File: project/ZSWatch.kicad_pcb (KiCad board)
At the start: 4 copper layers, 41 x 38 mm, 92 parts, among them IC101 nPM1300-QEXX, IC201 APDS-9306-065, IC202 BMI270, IC203 BMP581, IC204 LIS2MDLTR, IC205 BME688, IC301 ESDALC6V1W5, IC302 FAN5622SX, IC303 MX25U51245GZ4I00, IC304 TS3USB221A, IC305 NTS0104GU12, IC306 DRV2603RUNT, IC307 RV-8263-C8, M301 NORA-B106, Q201 DMG1013UW-7, Q301 BC817W, Q302 PMZ550UNEYL, Q303 PMZ550UNEYL, X101 BATTERY, X301 DOCK, X302 GC9A01A_CST816S, X303 M+, X304 M-

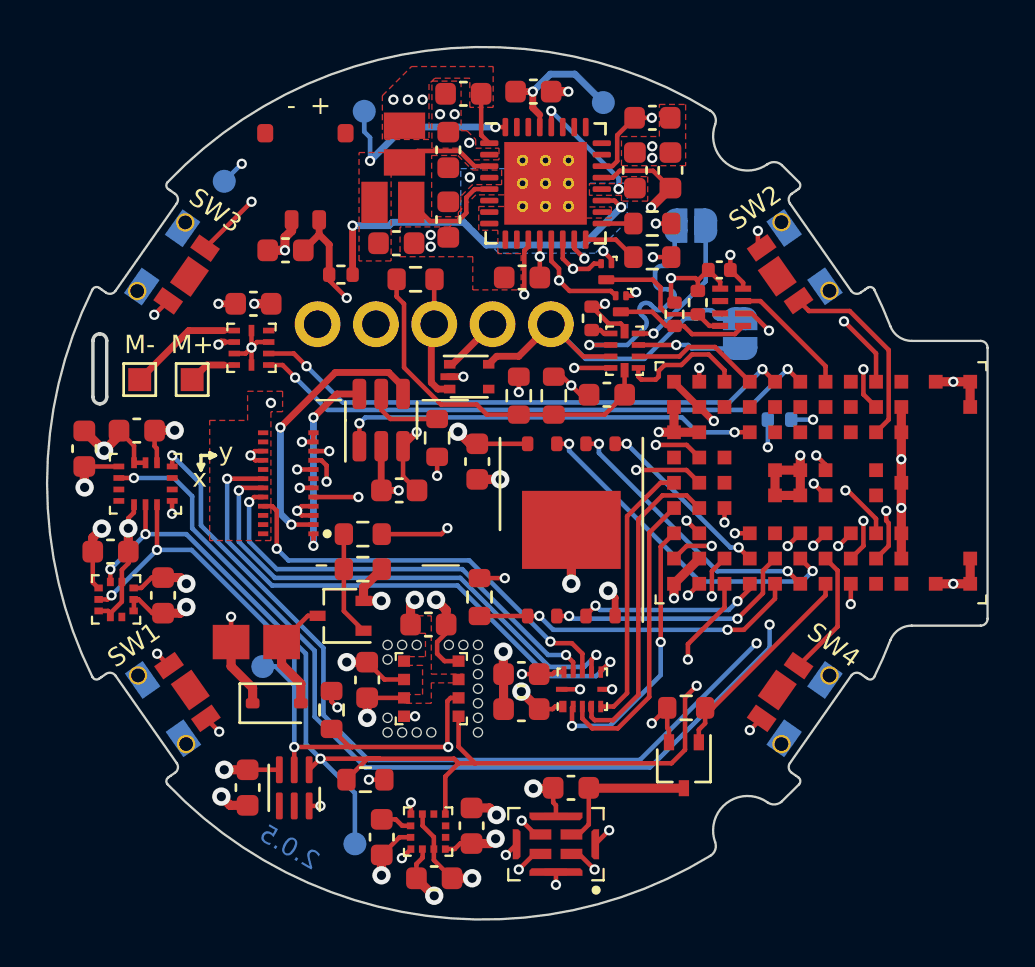
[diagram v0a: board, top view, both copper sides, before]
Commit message: PCB: Remove BME688 and USB switch
- Implement #106
- Remove USB switch and the required components

Signed-off-by: Daniel Kampert <danielkampert@kampis-elektroecke.de>
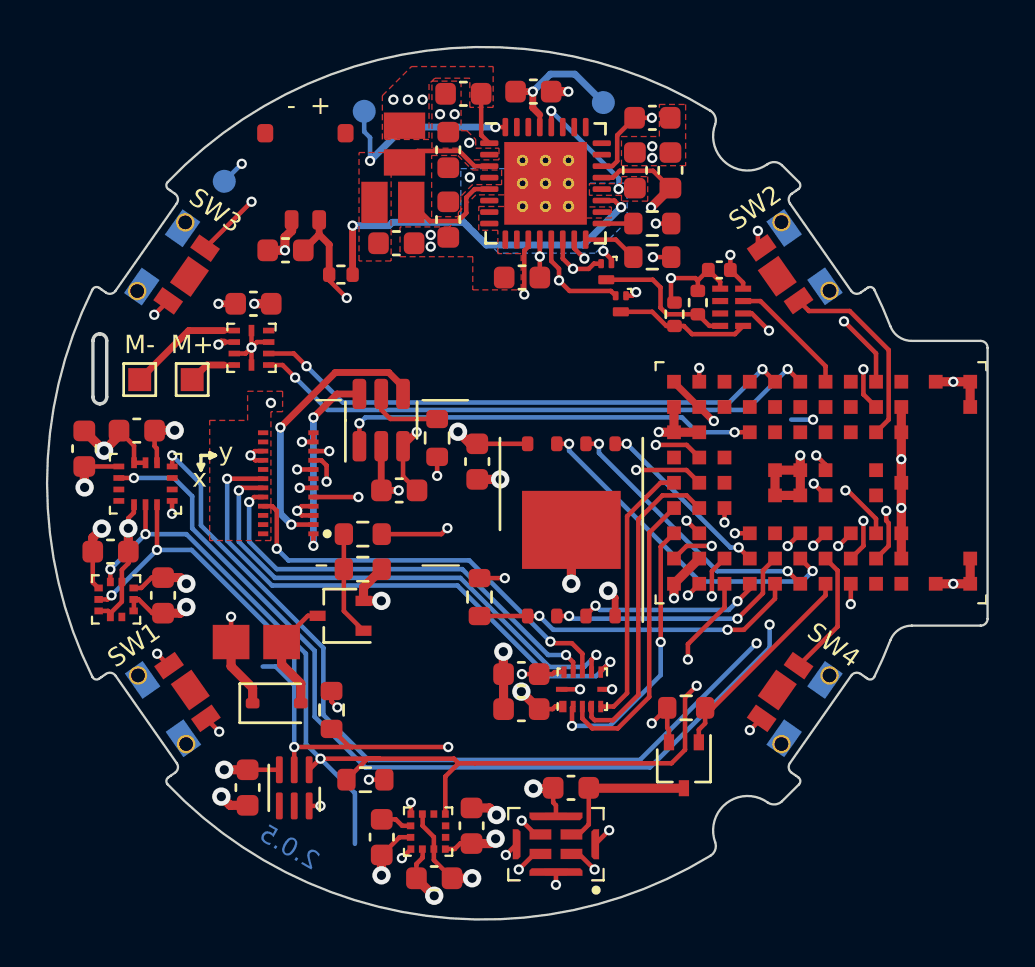
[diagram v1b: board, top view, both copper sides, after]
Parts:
- removed C210, C212, C303: 100n, Capacitor_SMD:C_0603_1608Metric
- removed IC205: BME688, Package_LGA_Kampi:Bosch_LGA-8_3x3mm_P0.8mm_ClockwisePinNumbering
- removed IC301: ESDALC6V1W5, Package_TO_SOT_SMD:SOT-665
- removed IC304: TS3USB221A, Package_QFN:UQFN-10_1.55x2.05mm_P0.5mm
- removed JP301, JP302: ~, Jumper:SolderJumper-2_P1.3mm_Open_RoundedPad1.0x1.5mm
- removed R305: 100k, Resistor_SMD:R_0603_1608Metric
- removed R306, R310: 0R, Resistor_SMD:R_0402_1005Metric
- removed R308: 270R, Resistor_SMD:R_0603_1608Metric
- removed R312: 100R, Resistor_SMD:R_0603_1608Metric
- removed TP201: SCL, TestPoint:TestPoint_Pad_D1.0mm
- removed TP202: SDA, TestPoint:TestPoint_Pad_D1.0mm
- removed X301: DOCK, Pomagtor:RD90_LZH0230529-004_DJ-5PIN_PH2_54
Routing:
- net SEL-SWD: track 25.1 -> 0.00 mm, vias 2 -> 0
- net D_N/SWDIO: track 18.5 -> 0.00 mm, vias 1 -> 0
- net VBUS: track 22.4 -> 4.62 mm
- net D_P/SWDCLK: track 16.6 -> 0.00 mm
- net /MCU/V_SWITCH: track 15.9 -> 0.00 mm
- net GND: track 87.6 -> 75.3 mm, vias 55 -> 49
- net SWDIO: track 23.7 -> 14.0 mm, vias 2 -> 1
- net /MCU/VBUS-MCU: track 25.3 -> 16.1 mm, vias 3 -> 2
- net SWDCLK: track 21.4 -> 14.6 mm, vias 2 -> 1
- net USB-D_N: track 5.65 -> 0.00 mm
- net USB-D_P: track 5.57 -> 0.00 mm
- net +1V8: track 47.2 -> 43.5 mm, vias 25 -> 23
- net /MCU/SENSOR-SDA: track 82.8 -> 80.3 mm
- net /MCU/SENSOR-SCL: track 88.9 -> 86.5 mm
- net Net-(IC304-~{OE}): track 0.90 -> 0.00 mm
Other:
- outline, holes or cut-outs redrawn

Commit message: Project: Port to KiCad 9
- Port to KiCad 9.0.1

Closes #101

Signed-off-by: Daniel Kampert <danielkampert@kampis-elektroecke.de>
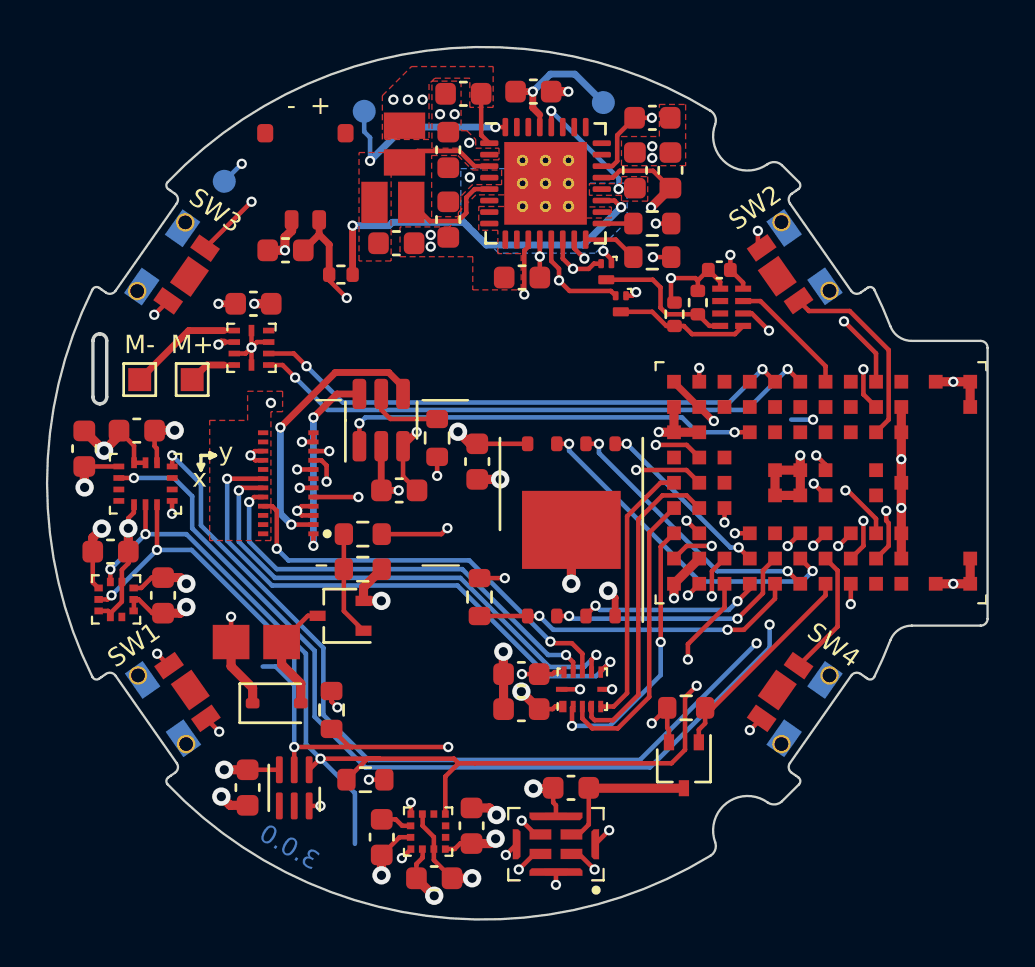
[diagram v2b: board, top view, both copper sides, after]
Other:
- board text added: "3.0.${REVISION}"
- board text removed: "2.0.${REVISION}"
